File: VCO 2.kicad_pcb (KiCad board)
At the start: 2 copper layers, 185.7 x 142.5 mm, 132 parts, among them J1 OUT 1x4s, J10 IN 1x6h, J11 SYNC, J12 PWM, J13 CV, J14 1VOct, J15 FM, J17 OCT 1x6s, J18 CV 1x6s, J19 CV 1x6h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

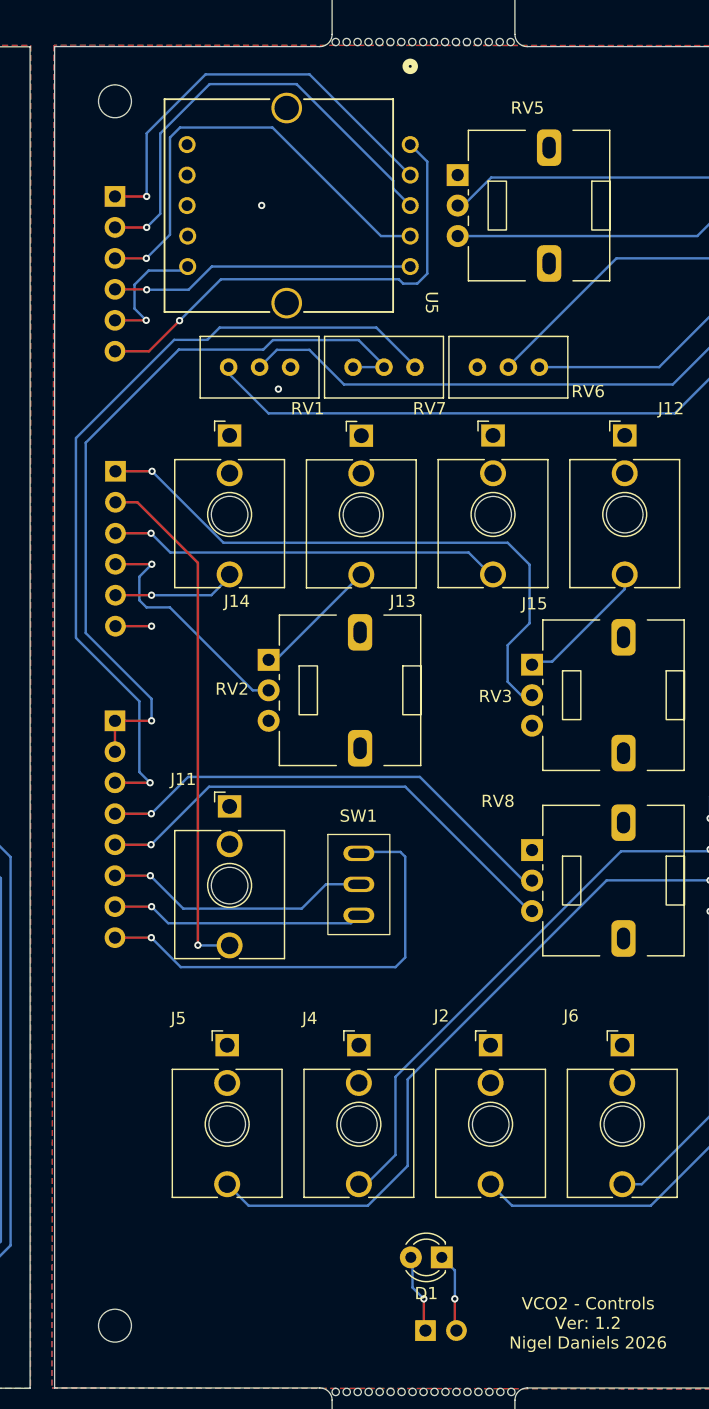
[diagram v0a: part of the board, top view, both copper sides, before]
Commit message: Corrected connections for levels and octave switch
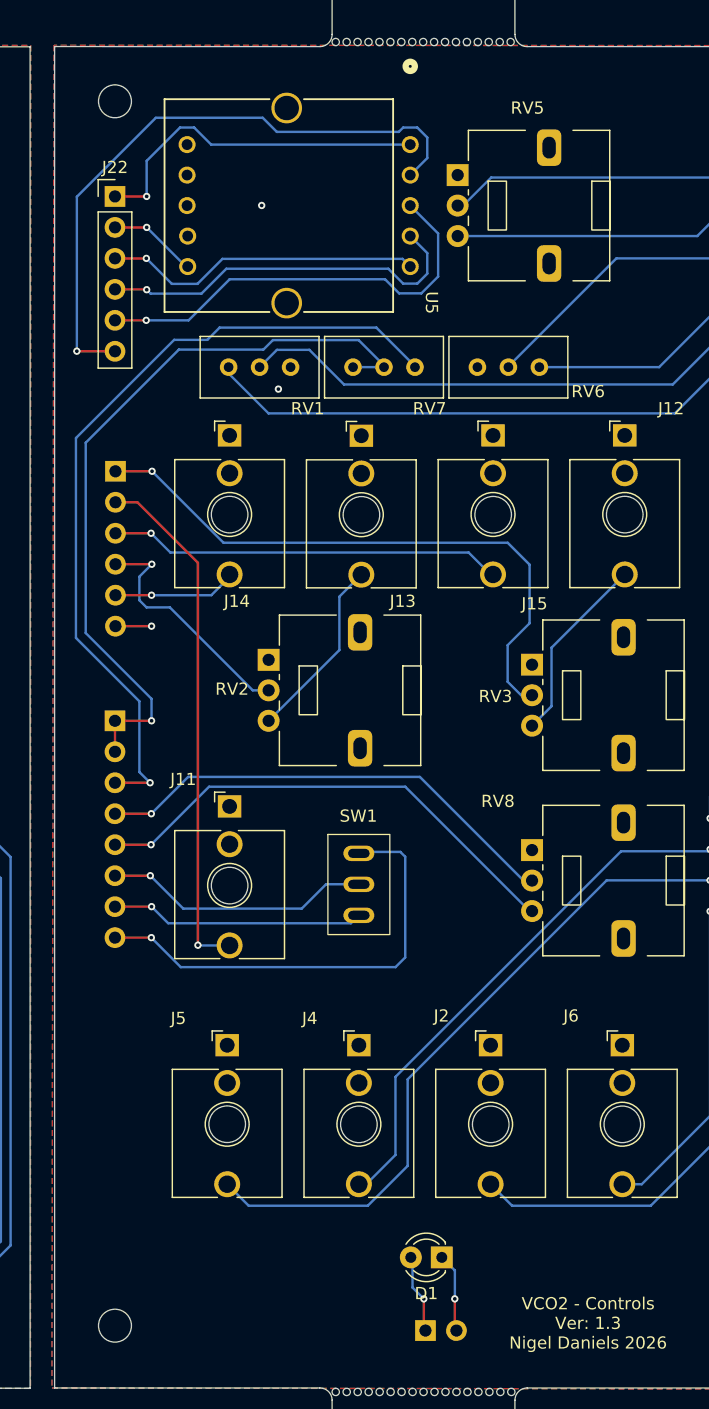
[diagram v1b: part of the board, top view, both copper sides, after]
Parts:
- J22: moved to F.Cu
- R41: value 9.1K -> 9K1
- R8: value 220 -> 220R
- turned J22 to 0 degrees
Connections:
- RV2 pad 1: Net-(J13-PadT) -> GND
- RV2 pad 3: GND -> Net-(J13-PadT)
- RV3 pad 1: Net-(J12-PadT) -> GND
- RV3 pad 3: GND -> Net-(J12-PadT)
- U5 pad 1: Net-(J22-Pin_6) -> Net-(J22-Pin_1)
- U5 pad 2: Net-(J22-Pin_1) -> Net-(J22-Pin_6)
- U5 pad 3: Net-(J22-Pin_2) -> Net-(J22-Pin_5)
- U5 pad 4: Net-(J22-Pin_3) -> Net-(J22-Pin_4)
- U5 pad 5: Net-(J22-Pin_4) -> Net-(J22-Pin_3)
- U5 pad 6: Net-(J22-Pin_5) -> Net-(J22-Pin_2)
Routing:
- net Net-(J22-Pin_2): track 37.4 -> 7.29 mm
- net Net-(J22-Pin_5): track 10.9 -> 35.7 mm
- net Net-(J22-Pin_6): track 39.7 -> 51.8 mm
- net Net-(J22-Pin_3): track 37.0 -> 26.2 mm
- net Net-(J22-Pin_4): track 25.0 -> 31.1 mm
- net Net-(J22-Pin_1): track 34.8 -> 28.8 mm
- net Net-(J13-PadT): track 10.6 -> 15.1 mm
- net Net-(J12-PadT): track 11.4 -> 15.5 mm
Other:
- board text added: "1.3"
- board text added: "VCO2 - Controls Ver: 1.3 Nigel Daniels 2026"
- board text added: "VCO2 - Front Panel Ver: 1.3 Nigel Daniels 2026"
- board text added: "VCO2 - Main Board Ver: 1.3 Nigel Daniels 2026"
- board text removed: "1.2"
- board text removed: "VCO2 - Controls Ver: 1.2 Nigel Daniels 2026"
- board text removed: "VCO2 - Front Panel Ver: 1.2 Nigel Daniels 2026"
- board text removed: "VCO2 - Main Board Ver: 1.2 Nigel Daniels 2026"

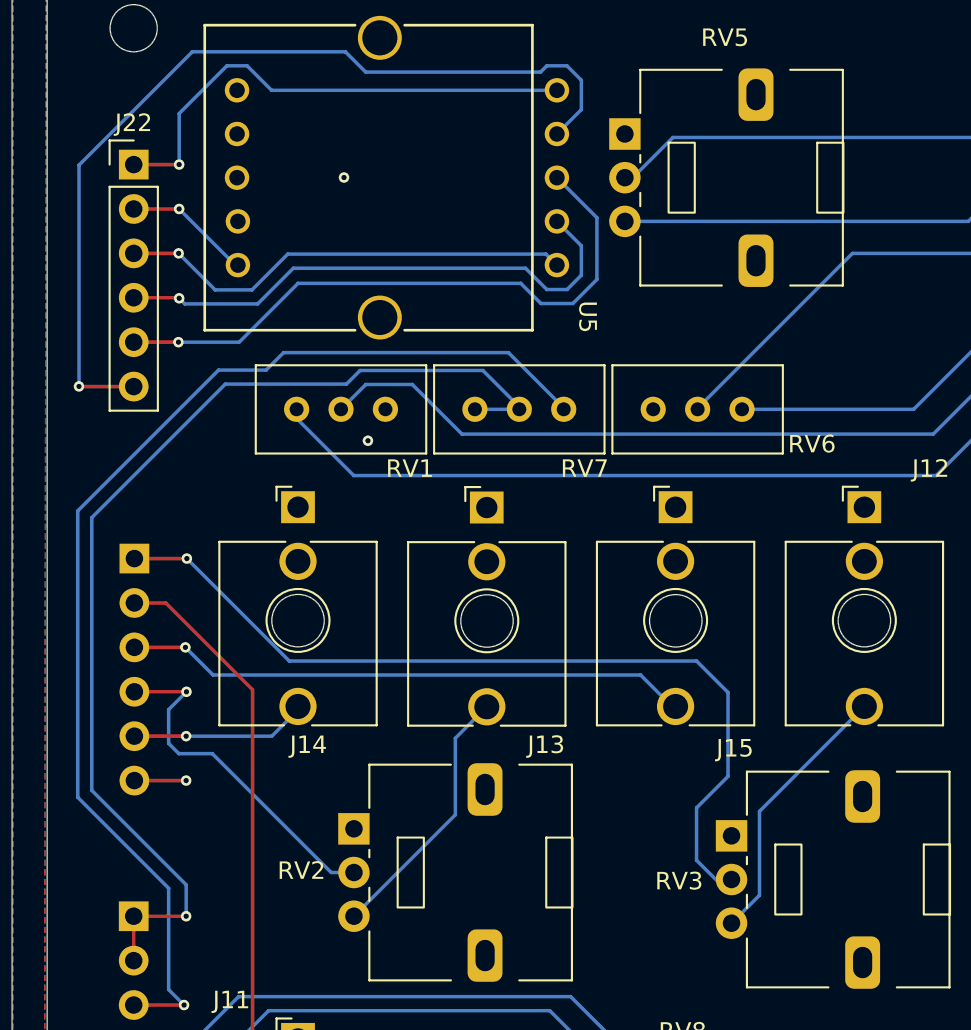
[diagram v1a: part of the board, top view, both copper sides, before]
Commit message: Updated to correct for DRC check and refreshed fab files
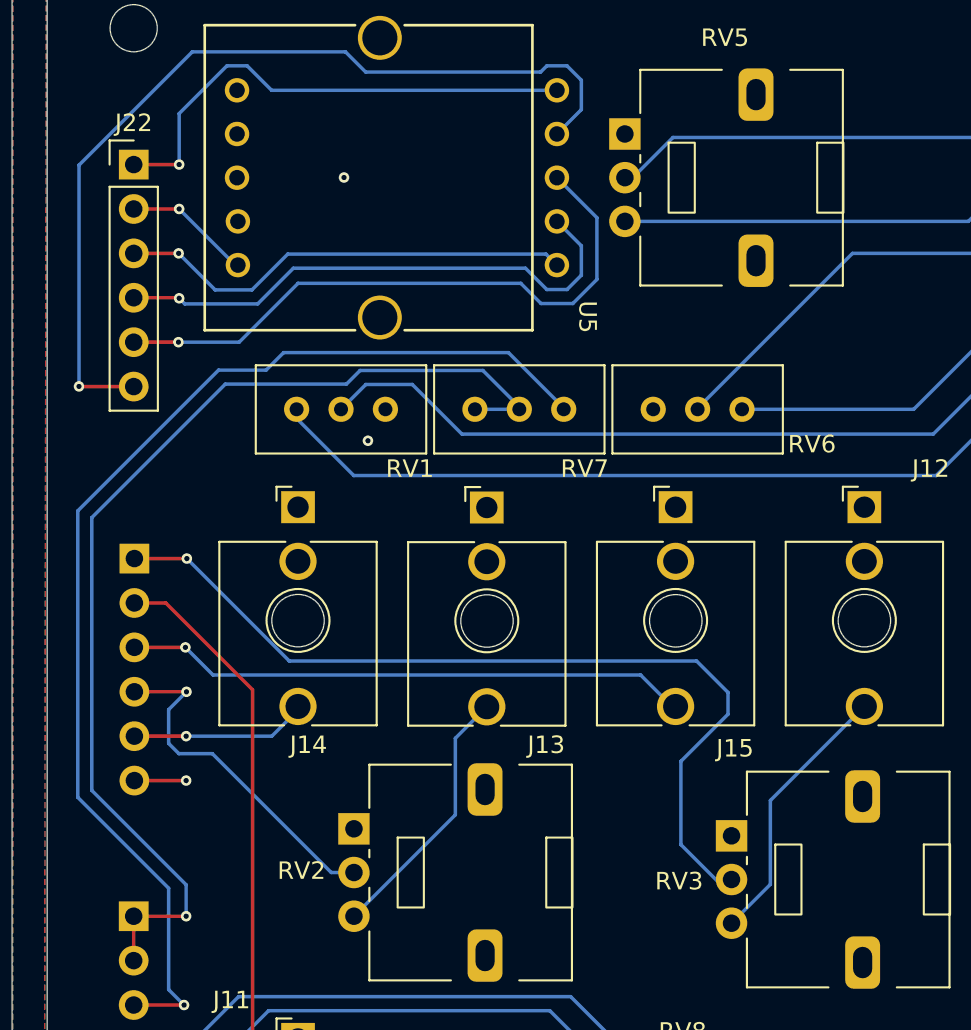
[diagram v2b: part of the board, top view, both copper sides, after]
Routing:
- net Net-(J10-Pin_1): track 50.6 -> 51.3 mm
